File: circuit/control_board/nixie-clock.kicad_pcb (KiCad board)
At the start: 2 copper layers, 101.6 x 43.7 mm, 44 parts, among them IC1 ATMEGA328-P, P1 CONN_2, P10 CONN_2, P2 CONN_2, P3 CONN_4, P4 CONN_4, P5 CONN_8, P6 CONN_12, P7 CONN_2, P8 CONN_2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

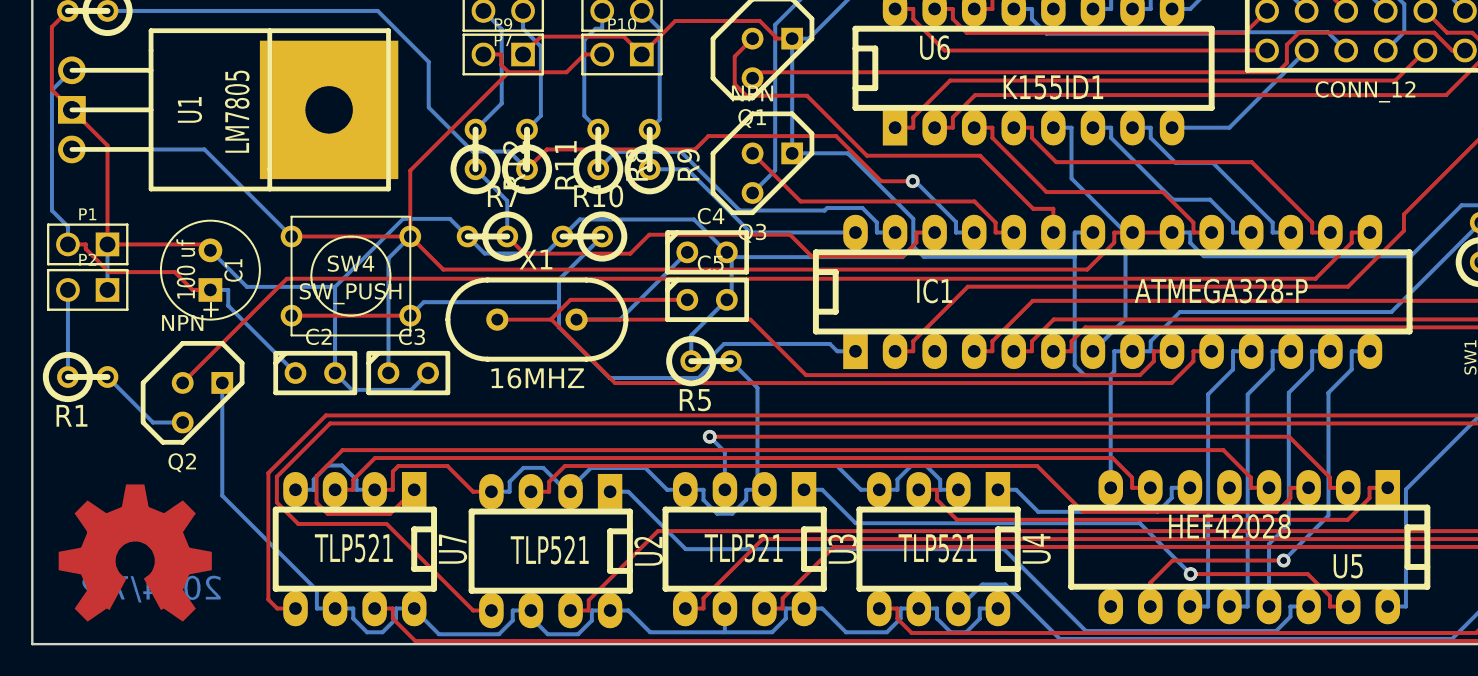
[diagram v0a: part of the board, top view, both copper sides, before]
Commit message: Control board: Add two screw drill hole
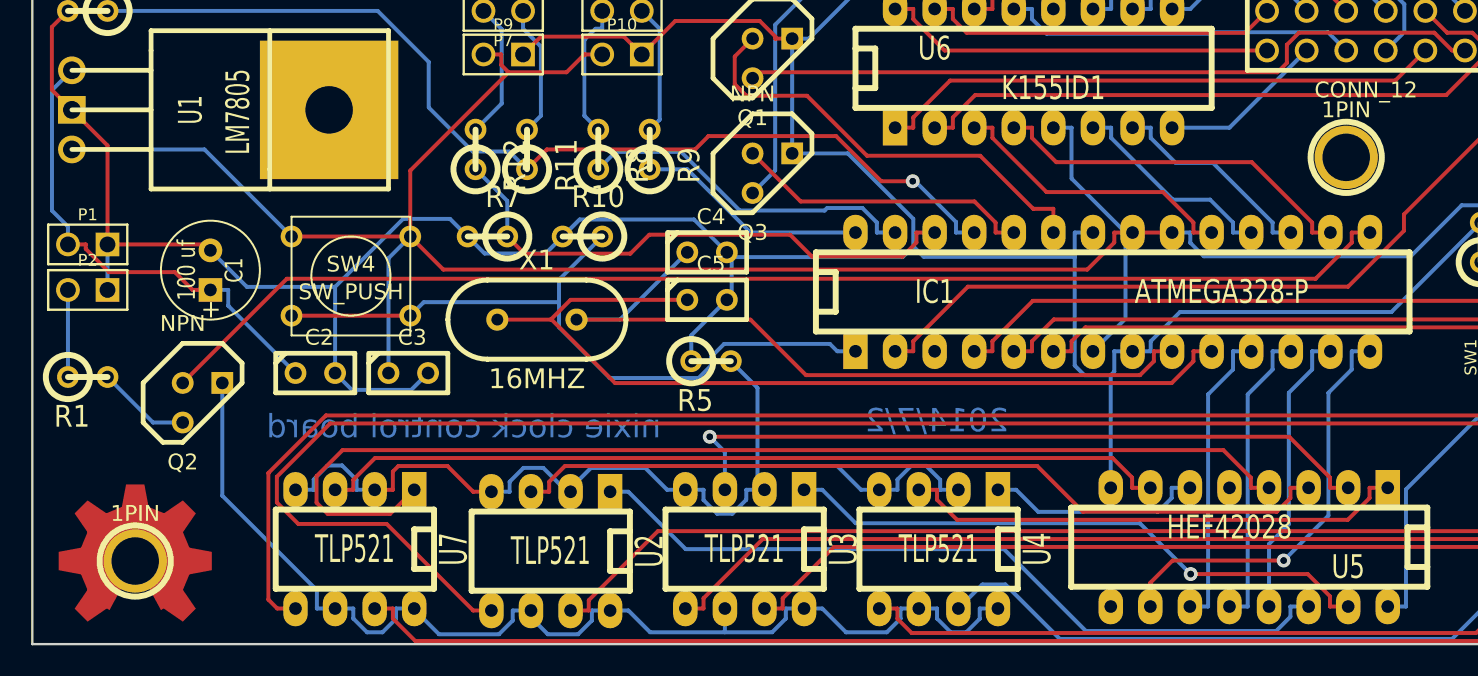
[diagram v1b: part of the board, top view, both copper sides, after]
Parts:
- added 1PIN: P***, Connect:1pin, F.Cu at (183.9, 93.5)
- added 1PIN: P***, Connect:1pin, F.Cu at (106.2, 119.4)
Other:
- board text added: "nixie clock control board"

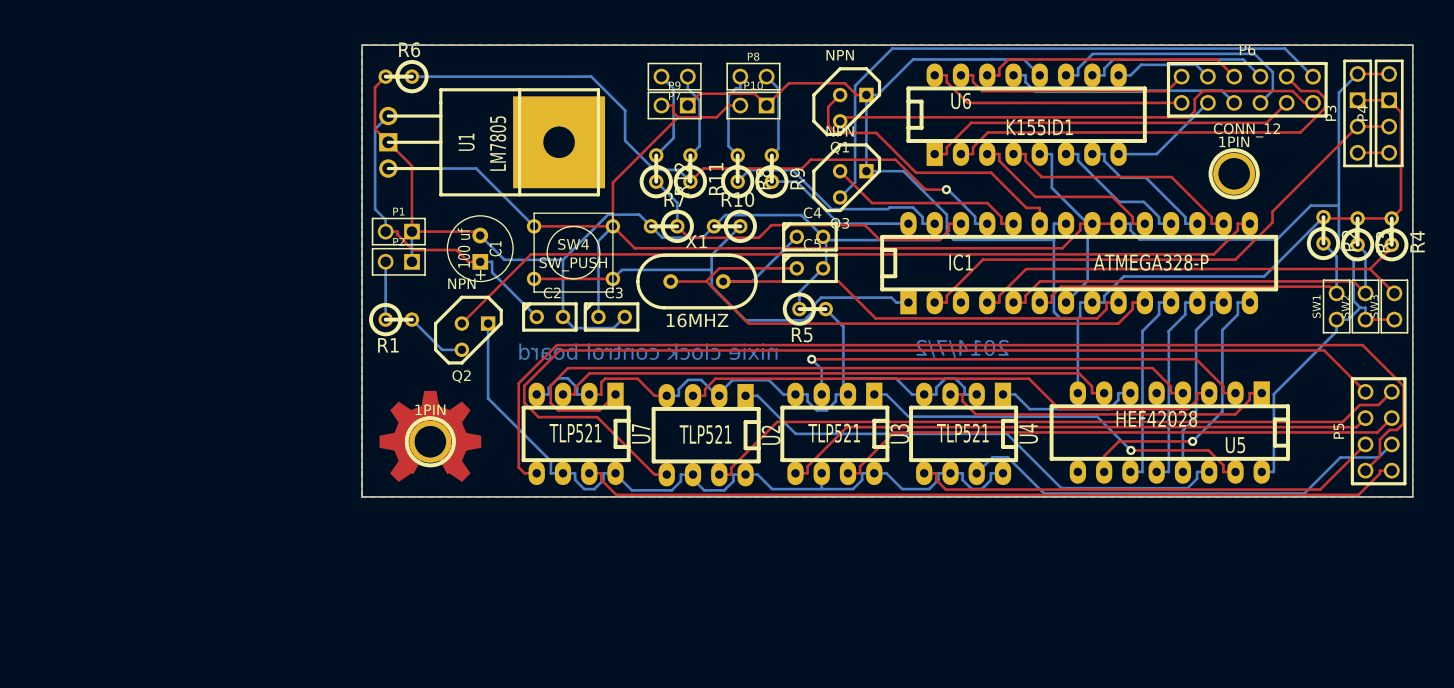
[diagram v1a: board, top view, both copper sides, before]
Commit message: Control board: Remove the coper zone and adjust the track line
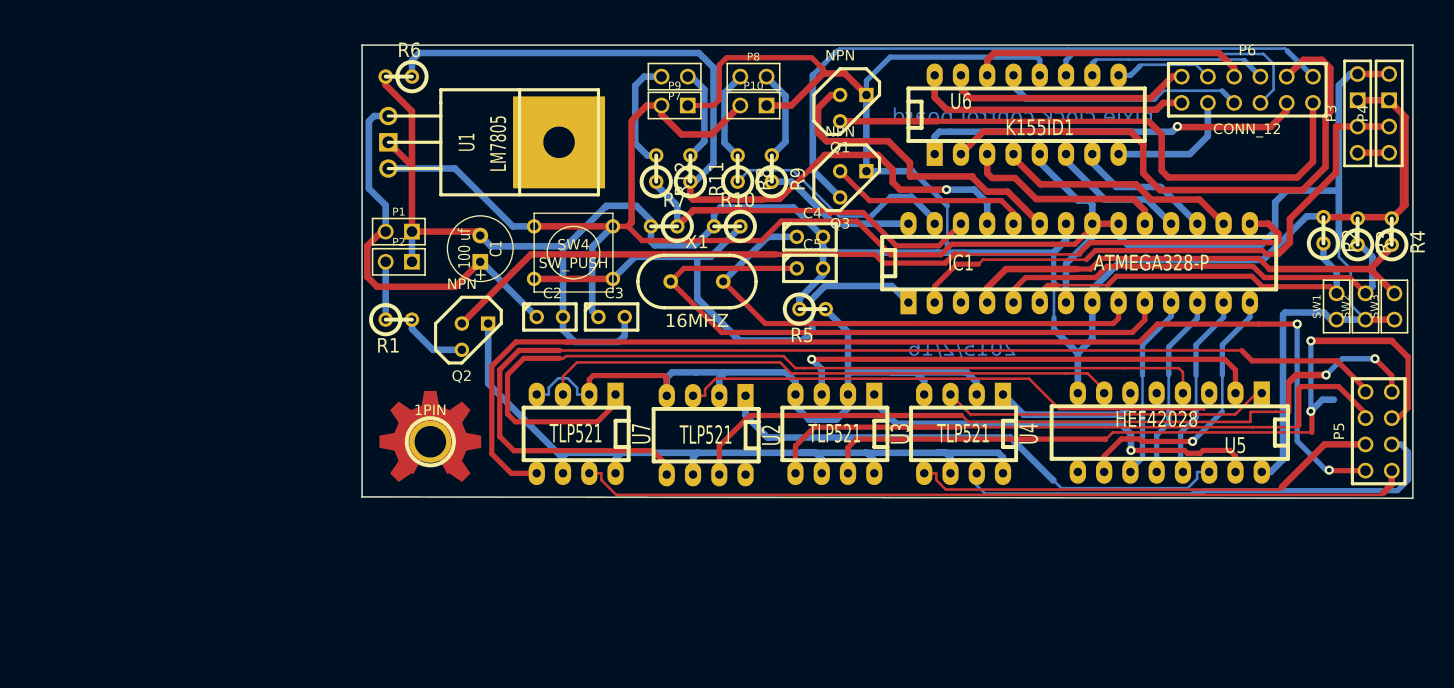
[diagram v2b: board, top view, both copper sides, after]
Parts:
- removed the 1PIN at (183.9, 93.5)
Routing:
- net GND: track 235.9 -> 285.2 mm
- net N-0000055: track 46.5 -> 88.9 mm
- net Reset: track 46.3 -> 85.6 mm
- net N-0000010: track 55.2 -> 79.9 mm, vias 0 -> 2
- net 5V: track 201.4 -> 218.8 mm
- net N-0000060: track 22.9 -> 39.5 mm
- net MP3 Tx: track 65.4 -> 80.6 mm
- net N-0000037: track 43.0 -> 56.1 mm
- net N-0000047: track 72.1 -> 84.9 mm
- net N-000003: track 63.8 -> 73.0 mm
- net N-000002: track 102.7 -> 111.0 mm
- net N-0000044: track 48.1 -> 56.3 mm
- net N-0000065: track 30.9 -> 38.8 mm
- net Mode button: track 45.3 -> 53.0 mm
- net N-0000012: track 68.7 -> 76.4 mm, vias 0 -> 2
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- removed copper zone on B.Cu, net (none)
- removed copper zone on F.Cu, net (none)
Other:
- board size 101.6 x 43.7 mm -> 101.6 x 43.8 mm
- net class 25mil added: clearance 0.254, trace_width 0.635, via_dia 0.889, via_drill 0.635
- board text added: "2015/2/16"
- board text removed: "2014/7/2"

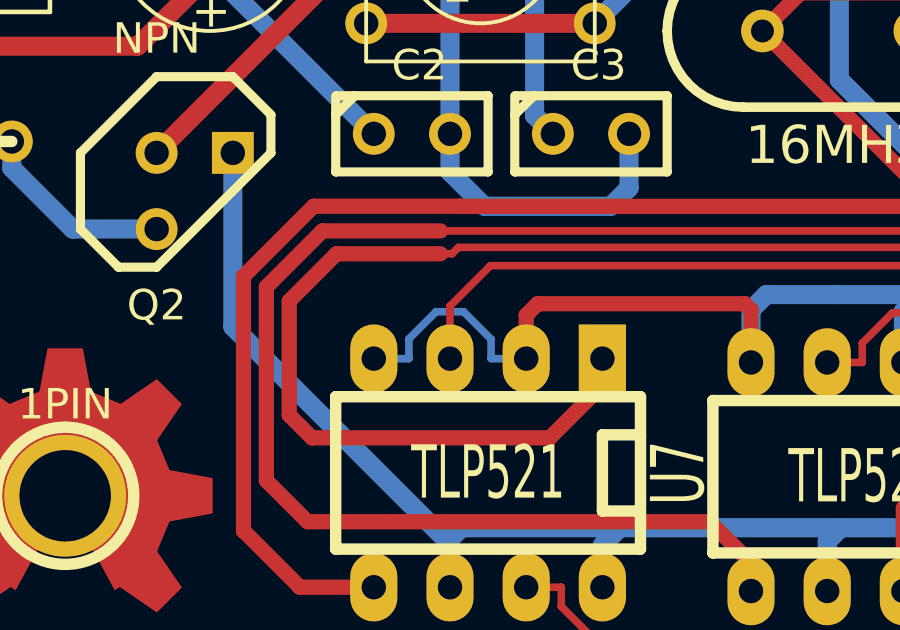
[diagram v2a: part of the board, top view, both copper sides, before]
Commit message: Control board: Adjust track line width
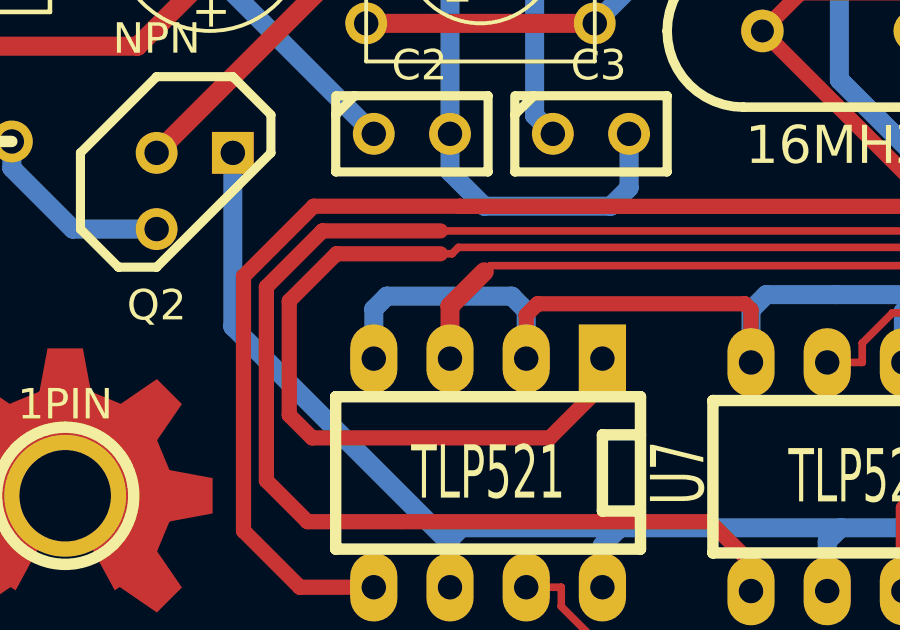
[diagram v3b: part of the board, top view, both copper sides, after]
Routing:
- net N-000003: track 73.0 -> 74.6 mm

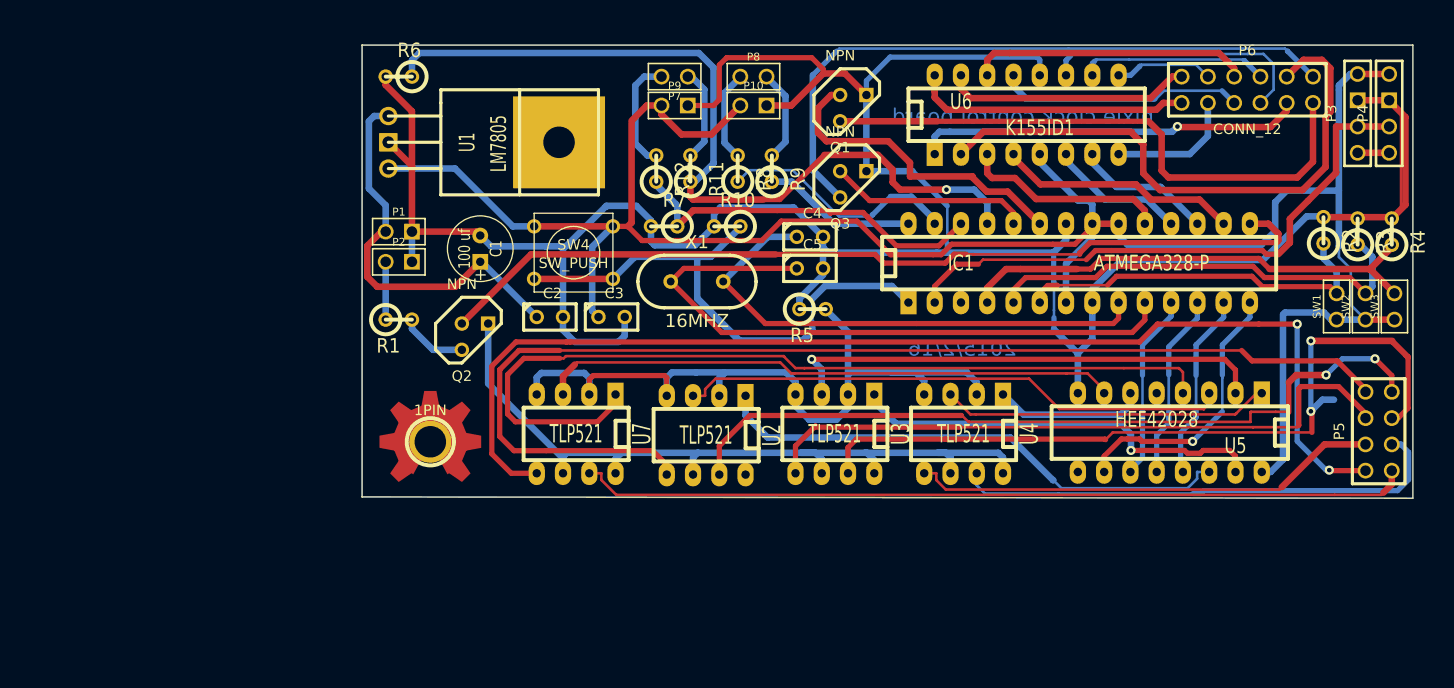
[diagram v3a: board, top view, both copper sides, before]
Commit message: Control board: Adjust track line, pad size and via size
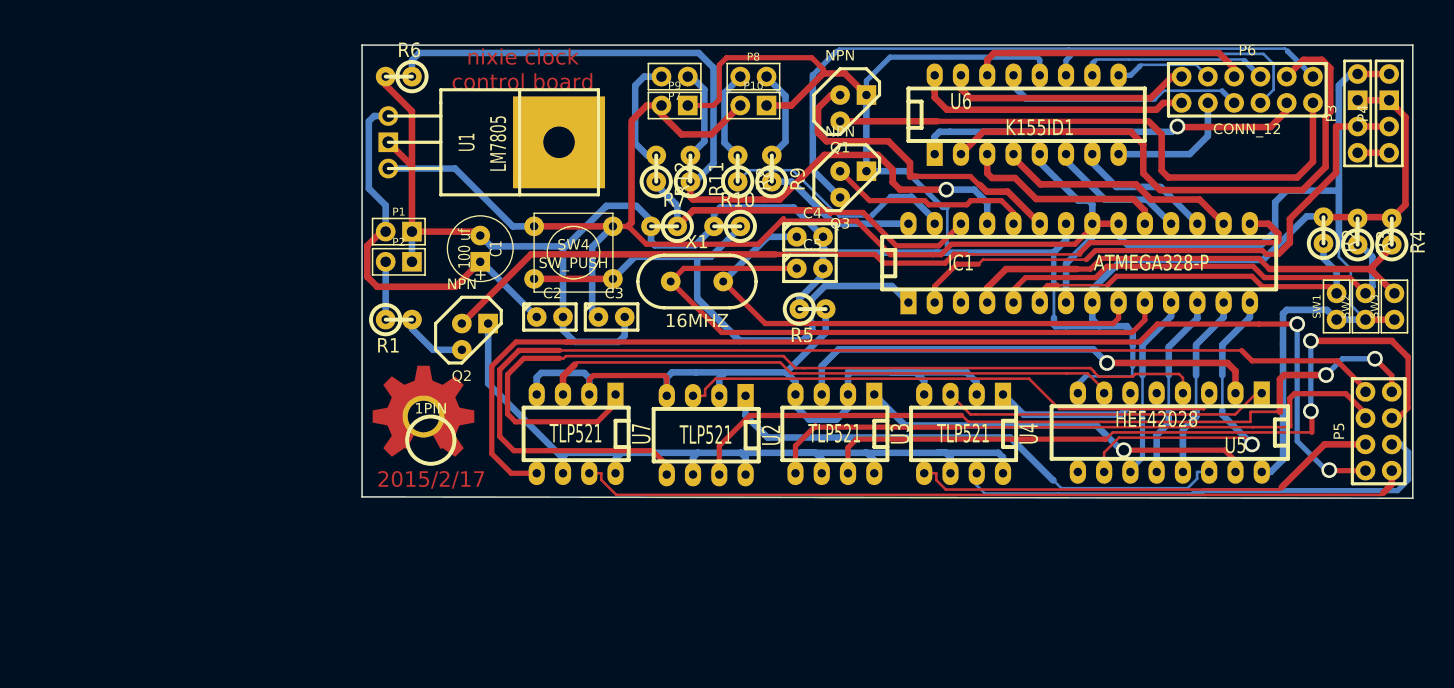
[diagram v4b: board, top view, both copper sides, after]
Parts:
- moved OSHW_COPPER_10MM 2.53 mm to (105.5, 116.9)
- moved 1PIN 0.16 mm to (106.2, 119.2)
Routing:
- net N-0000055: track 88.9 -> 49.7 mm
- net Digit A0: track 30.4 -> 43.5 mm
- net Digit A2: track 24.7 -> 34.4 mm
- net Digit A1: track 23.4 -> 30.6 mm
- net Digit A3: track 26.7 -> 33.6 mm
- net Left dot: track 19.5 -> 24.6 mm
- net GND: track 285.2 -> 289.9 mm
- net N-0000010: track 79.9 -> 77.2 mm
- net N-000001: track 75.5 -> 77.8 mm
- net N-0000054: track 40.5 -> 38.7 mm
- net MP3 Tx: track 80.6 -> 82.1 mm
- net 5V: track 218.8 -> 219.9 mm
- net N-000003: track 74.6 -> 75.3 mm
- net N-0000011: track 64.8 -> 64.1 mm
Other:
- board text added: "2015/2/17"
- board text removed: "2015/2/16"

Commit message: Control board: Optimize TLP521 route
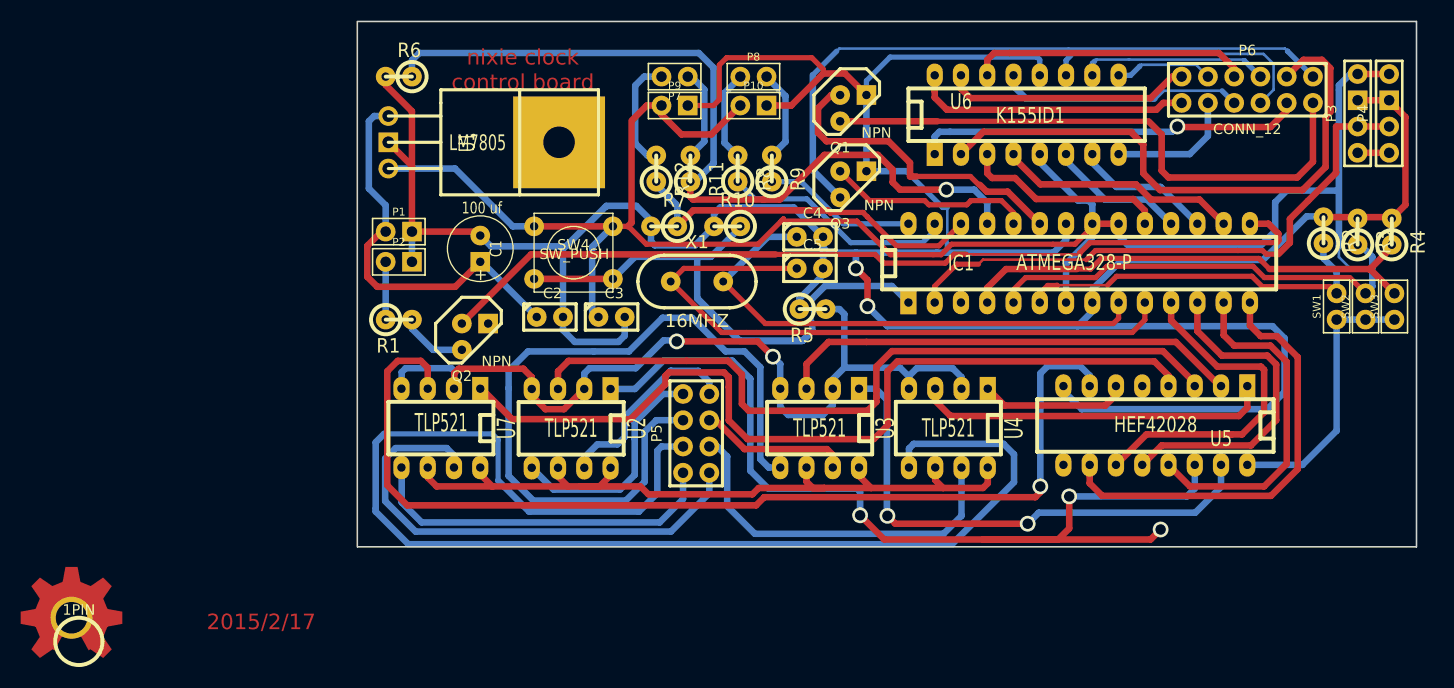
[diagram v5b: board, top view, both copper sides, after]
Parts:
- moved P5 66.0 mm to (131.9, 118.6)
- moved 1PIN 39.2 mm to (72.2, 138.7)
- moved OSHW_COPPER_10MM 39.2 mm to (71.5, 136.4)
- moved U7 13.1 mm to (107.2, 118.1)
- moved U2 13.1 mm to (119.8, 118.1)
- moved U3 1.58 mm to (143.8, 118.1)
- moved U4 1.58 mm to (156.3, 118.1)
- moved U5 1.56 mm to (176.3, 117.8)
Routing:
- net N-000002: track 111.0 -> 23.1 mm
- net N-000007: track 45.5 -> 128.0 mm
- net N-000004: track 112.3 -> 35.1 mm, vias 2 -> 0
- net N-0000010: track 77.2 -> 14.5 mm, vias 2 -> 0
- net N-0000012: track 76.5 -> 19.4 mm, vias 2 -> 0
- net N-000005: track 50.7 -> 95.4 mm, vias 0 -> 3
- net N-0000050: track 56.0 -> 100.1 mm, vias 0 -> 1
- net GND: track 289.9 -> 328.4 mm, vias 0 -> 2
- net N-000009: track 80.6 -> 48.6 mm
- net N-000006: track 53.4 -> 73.7 mm
- net N-000003: track 75.3 -> 87.8 mm, vias 0 -> 2
- net N-000008: track 48.4 -> 36.1 mm
- net N-0000054: track 38.7 -> 50.6 mm, vias 1 -> 2
- net N-0000011: track 64.1 -> 73.7 mm
- net 5V: track 219.9 -> 212.8 mm
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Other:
- board size 101.6 x 43.8 mm -> 102.4 x 50.8 mm
